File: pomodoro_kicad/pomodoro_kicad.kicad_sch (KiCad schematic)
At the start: 48 parts, among them J1 LiPO PH2.0, J10 LED_VCC, J11 LED_DATA, J12 LED_GND, J2 Conn_01x04, J3 VDD, J4 GND, J5 SCK, J6 WS, J7 SD, J8 L/R, J9 USB_C_Receptacle_USB2.0_16P, Q1 IRLML6402, SW1 RotaryEncoder_Switch, U1 AP2112K-3.3, U2 MCP73831-2-OT, U3 ESP32-S3-WROOM-1-N16R8

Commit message: Assign footprints with actual parts
assigned:
- capacitors
- LEDs
- diode
- resistors
- push button
- usb receptacle
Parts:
- removed C13: 220uF, Capacitor_SMD:C_0603_1608Metric, symbol Device:C_Small
- added C14: 220uF, Capacitor_SMD:CP_Elec_6.3x7.7, symbol Device:C_Polarized_Small
- C1, C10, C11, C12, C2, C3, C4, C6, C7, C8, C9: footprint Capacitor_SMD:C_0603_1608Metric -> Capacitor_SMD:C_0402_1005Metric
- C5: value 100nF -> 0.1uF; footprint Capacitor_SMD:C_0603_1608Metric -> Capacitor_SMD:C_0402_1005Metric
- D3: footprint Diode_SMD:D_SMA -> Diode_SMD:D_SOD-123F
- J9: footprint Connector_USB:USB_C_Receptacle_HRO_TYPE-C-31-M-12 -> _Footprints:SAMESKY_UJ20-C-H-G-SMT-1-P16-TR
- SW1: footprint customFootprints:rotaryEncoder -> _Footprints:rotaryEncoder
- SW2, SW3: footprint Button_Switch_SMD:SW_SPST_PTS645Sx43SMTR92 -> Button_Switch_SMD:SW_Tactile_SPST_NO_Straight_CK_PTS636Sx25SMTRLFS
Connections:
- net GND: now also C14.2
- net VSYS: now also C14.1
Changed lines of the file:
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@@
 			)
 		)
-		(property "Footprint" "customFootprints:rotaryEncoder"
+		(property "Footprint" "_Footprints:rotaryEncoder"
 			(at 44.704 162.56 0)
 			(hide yes)
@@
 			)
 		)
-		(property "Footprint" "Button_Switch_SMD:SW_SPST_PTS645Sx43SMTR92"
+		(property "Footprint" "Button_Switch_SMD:SW_Tactile_SPST_NO_Straight_CK_PTS636Sx25SMTRLFS"
 			(at 86.36 69.85 0)
 			(hide yes)
@@
 			)
 		)
-		(property "Footprint" "Capacitor_SMD:C_0603_1608Metric"
+		(property "Footprint" "Capacitor_SMD:C_0402_1005Metric"
 			(at 119.38 156.21 0)
 			(hide yes)
@@
 			)
 		)
-		(property "Footprint" "Capacitor_SMD:C_0603_1608Metric"
+		(property "Footprint" "Capacitor_SMD:C_0402_1005Metric"
 			(at 95.25 27.94 0)
 			(hide yes)
@@
 			)
 		)
-		(property "Footprint" "Capacitor_SMD:C_0603_1608Metric"
+		(property "Footprint" "Capacitor_SMD:C_0402_1005Metric"
 			(at 26.67 57.15 0)
 			(hide yes)
@@
 			)
 		)
-		(property "Value" "100nF"
+		(property "Value" "0.1uF"
 			(at 40.894 187.452 90)
 			(show_name no)
@@
 			)
 		)
-		(property "Footprint" "Capacitor_SMD:C_0603_1608Metric"
+		(property "Footprint" "Capacitor_SMD:C_0402_1005Metric"
 			(at 43.18 182.88 0)
 			(hide yes)
@@
 			)
 		)
-		(property "Footprint" "Capacitor_SMD:C_0603_1608Metric"
+		(property "Footprint" "Capacitor_SMD:C_0402_1005Metric"
 			(at 24.13 158.75 0)
 			(hide yes)
@@
 			)
 		)
-		(property "Footprint" "Capacitor_SMD:C_0603_1608Metric"
+		(property "Footprint" "Capacitor_SMD:C_0402_1005Metric"
 			(at 26.67 64.77 0)
 			(hide yes)
@@
 			)
 		)
-		(property "Footprint" "Capacitor_SMD:C_0603_1608Metric"
+		(property "Footprint" "Capacitor_SMD:C_0402_1005Metric"
 			(at 22.86 87.63 0)
 			(hide yes)
@@
 			)
 		)
-		(property "Footprint" "Capacitor_SMD:C_0603_1608Metric"
+		(property "Footprint" "Capacitor_SMD:C_0402_1005Metric"
 			(at 104.14 149.86 0)
 			(hide yes)
@@
 			)
 		)
-		(property "Footprint" "Connector_USB:USB_C_Receptacle_HRO_TYPE-C-31-M-12"
+		(property "Footprint" "_Footprints:SAMESKY_UJ20-C-H-G-SMT-1-P16-TR"
 			(at 143.51 40.64 0)
 			(hide yes)
@@
 			)
 		)
-		(property "Footprint" "Capacitor_SMD:C_0603_1608Metric"
+		(property "Footprint" "Capacitor_SMD:C_0402_1005Metric"
 			(at 86.36 60.96 0)
 			(hide yes)
@@
 			)
 		)
-		(property "Footprint" "Diode_SMD:D_SMA"
+		(property "Footprint" "Diode_SMD:D_SOD-123F"
 			(at 164.465 96.52 0)
 			(hide yes)
@@
 	)
 	(symbol
+		(lib_id "Device:C_Polarized_Small")
+		(at 208.28 22.86 0)
+		(unit 1)
+		(body_style 1)
+		(exclude_from_sim no)
+		(in_bom yes)
+		(on_board yes)
+		(in_pos_files yes)
+		(dnp no)
+		(fields_autoplaced yes)
+		(property "Reference" "C14"
+			(at 210.82 21.0438 0)
+			(show_name no)
+			(do_not_autoplace no)
+			(effects
+				(font
+					(size 1.27 1.27)
+				)
+				(justify left)
+			)
+		)
+		(property "Value" "220uF"
+			(at 210.82 23.5838 0)
+			(show_name no)
+			(do_not_autoplace no)
+			(effects
+				(font
+					(size 1.27 1.27)
+				)
+				(justify left)
+			)
+		)
+		(property "Footprint" "Capacitor_SMD:CP_Elec_6.3x7.7"
+			(at 208.28 22.86 0)
+			(hide yes)
+			(show_name no)
+			(do_not_autoplace no)
+			(effects
+				(font
+					(size 1.27 1.27)
+				)
+			)
+		)
+		(property "Datasheet" ""
+			(at 208.28 22.86 0)
+			(hide yes)
+			(show_name no)
+			(do_not_autoplace no)
+			(effects
+				(font
+					(size 1.27 1.27)
+				)
+			)
+		)
+		(property "Description" "Polarized capacitor, small symbol"
+			(at 208.28 22.86 0)
+			(hide yes)
+			(show_name no)
+			(do_not_autoplace no)
+			(effects
+				(font
+					(size 1.27 1.27)
+				)
+			)
+		)
+		(pin "1"
+		)
+		(pin "2"
+		)
+		(instances
+			(project "pomodoro_kicad"
+				(path "/10c5c50b-7fce-4167-a001-e0e180833e3a"
+					(reference "C14")
+					(unit 1)
+				)
+			)
+		)
+	)
+	(symbol
 		(lib_id "Device:C_Small")
 		(at 86.36 78.74 270)
@@
 			)
 		)
-		(property "Footprint" "Capacitor_SMD:C_0603_1608Metric"
+		(property "Footprint" "Capacitor_SMD:C_0402_1005Metric"
 			(at 86.36 78.74 0)
 			(hide yes)
@@
 			)
 		)
-		(property "Footprint" "Capacitor_SMD:C_0603_1608Metric"
+		(property "Footprint" "Capacitor_SMD:C_0402_1005Metric"
 			(at 64.77 27.94 0)
 			(hide yes)
@@
 	)
 	(symbol
-		(lib_id "Device:C_Small")
-		(at 208.28 22.86 0)
-		(unit 1)
-		(body_style 1)
-		(exclude_from_sim no)
-		(in_bom yes)
-		(on_board yes)
-		(in_pos_files yes)
-		(dnp no)
-		(fields_autoplaced yes)
-		(property "Reference" "C13"
-			(at 210.82 21.5899 0)
-			(show_name no)
-			(do_not_autoplace no)
-			(effects
-				(font
-					(size 1.27 1.27)
-				)
-				(justify left)
-			)
-		)
-		(property "Value" "220uF"
-			(at 210.82 24.1299 0)
-			(show_name no)
-			(do_not_autoplace no)
-			(effects
-				(font
-					(size 1.27 1.27)
-				)
-				(justify left)
-			)
-		)
-		(property "Footprint" "Capacitor_SMD:C_0603_1608Metric"
-			(at 208.28 22.86 0)
-			(hide yes)
-			(show_name no)
-			(do_not_autoplace no)
-			(effects
-				(font
-					(size 1.27 1.27)
-				)
-			)
-		)
-		(property "Datasheet" ""
-			(at 208.28 22.86 0)
-			(hide yes)
-			(show_name no)
-			(do_not_autoplace no)
-			(effects
-				(font
-					(size 1.27 1.27)
-				)
-			)
-		)
-		(property "Description" "Unpolarized capacitor, small symbol"
-			(at 208.28 33.02 0)
-			(hide yes)
-			(show_name no)
-			(do_not_autoplace no)
-			(effects
-				(font
-					(size 1.27 1.27)
-				)
-			)
-		)
-		(pin "2"
-		)
-		(pin "1"
-		)
-		(instances
-			(project "pomodoro_kicad"
-				(path "/10c5c50b-7fce-4167-a001-e0e180833e3a"
-					(reference "C13")
-					(unit 1)
-				)
-			)
-		)
-	)
-	(symbol
 		(lib_id "power:GND")
 		(at 48.26 182.88 0)
@@
 			)
 		)
-		(property "Footprint" "Button_Switch_SMD:SW_SPST_PTS645Sx43SMTR92"
+		(property "Footprint" "Button_Switch_SMD:SW_Tactile_SPST_NO_Straight_CK_PTS636Sx25SMTRLFS"
 			(at 86.36 52.07 0)
 			(hide yes)
@@
 			)
 		)
-		(property "Footprint" "Capacitor_SMD:C_0603_1608Metric"
+		(property "Footprint" "Capacitor_SMD:C_0402_1005Metric"
 			(at 57.15 160.02 0)
 			(hide yes)

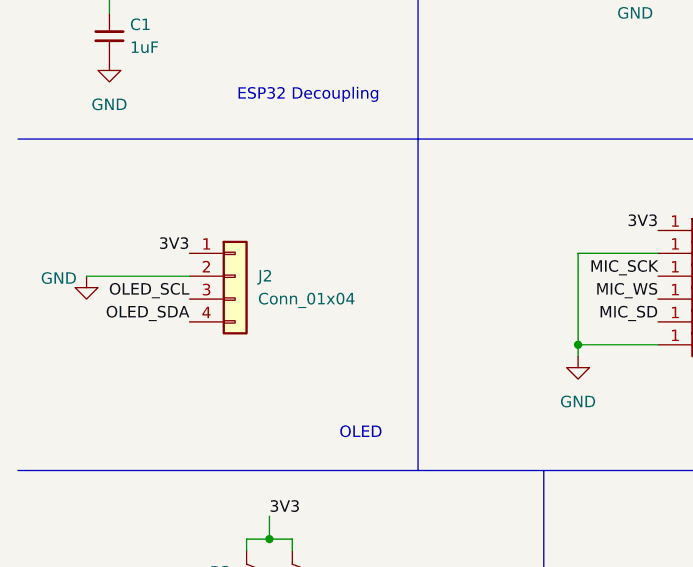
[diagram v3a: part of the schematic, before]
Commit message: Finish assigning footprints
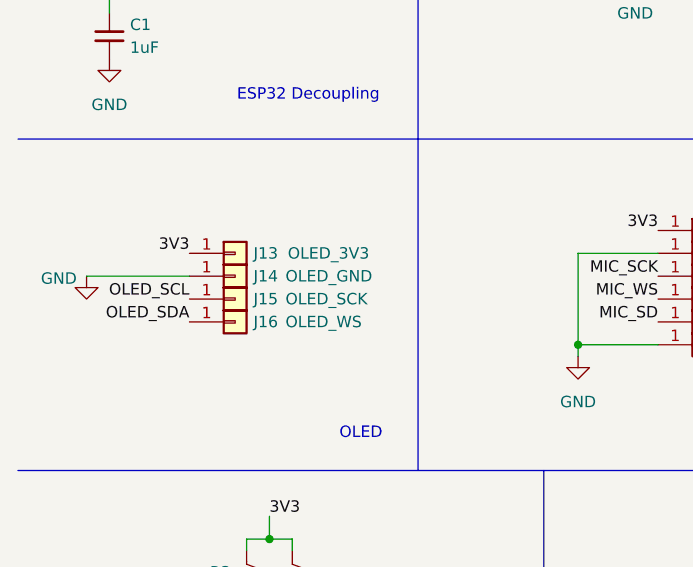
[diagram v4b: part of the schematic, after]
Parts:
- removed J2: Conn_01x04, Connector_PinSocket_2.54mm:PinSocket_1x04_P2.54mm_Vertical, symbol Connector_Generic:Conn_01x04
- added J13: OLED_3V3, TestPoint:TestPoint_THTPad_D2.0mm_Drill1.0mm, symbol Connector_Generic:Conn_01x01
- added J14: OLED_GND, TestPoint:TestPoint_THTPad_D2.0mm_Drill1.0mm, symbol Connector_Generic:Conn_01x01
- added J15: OLED_SCK, TestPoint:TestPoint_THTPad_D2.0mm_Drill1.0mm, symbol Connector_Generic:Conn_01x01
- added J16: OLED_WS, TestPoint:TestPoint_THTPad_D2.0mm_Drill1.0mm, symbol Connector_Generic:Conn_01x01
- J1: footprint Connector_JST:JST_PH_B2B-PH-K_1x02_P2.00mm_Vertical -> Connector_JST:JST_PH_S2B-PH-SM4-TB_1x02-1MP_P2.00mm_Horizontal
- Q1: footprint Package_TO_SOT_SMD:SOT-23 -> Package_TO_SOT_SMD:SOT-23-3
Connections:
- net 3V3: now also J13.1 (Pin_1)
- net GND: now also J14.1 (Pin_1)
- net OLED_SCL: now also J15.1 (Pin_1)
- net OLED_SDA: now also J16.1 (Pin_1)

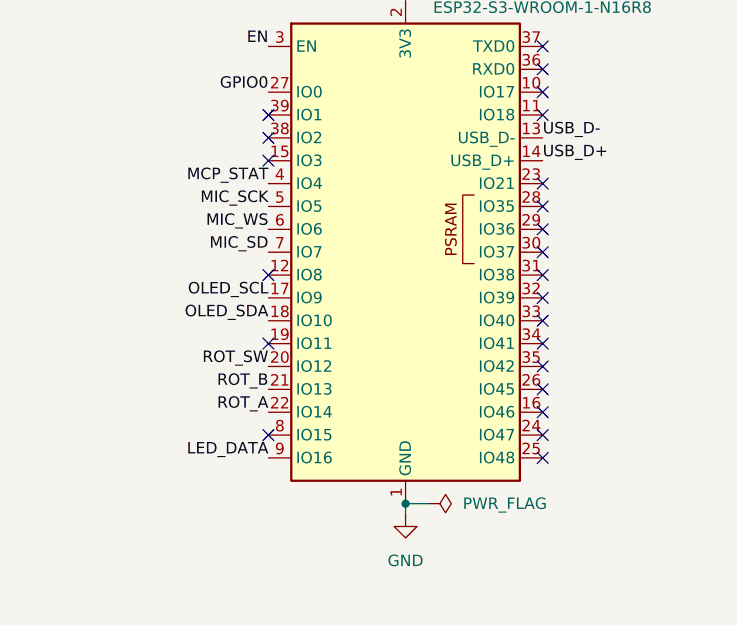
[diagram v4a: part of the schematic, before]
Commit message: Route PCB and update schematic pins for better connections
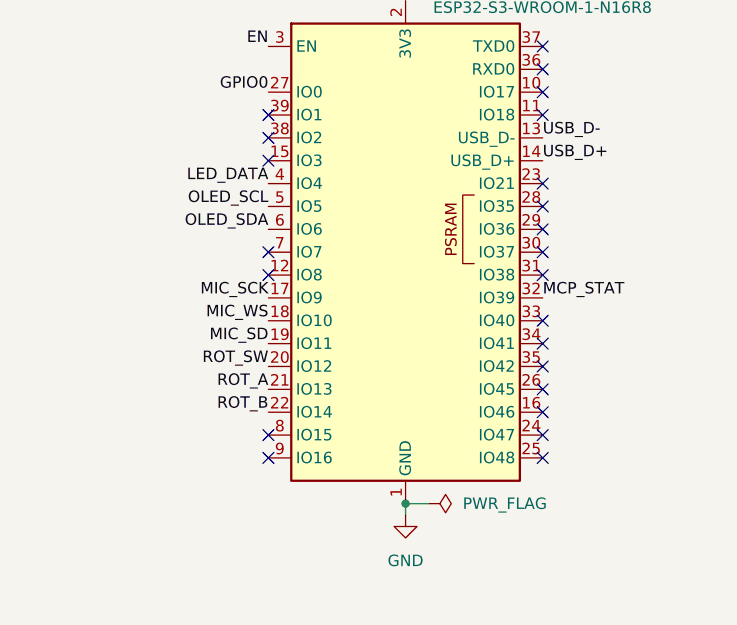
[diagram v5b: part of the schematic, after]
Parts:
- J9: footprint _Footprints:SAMESKY_UJ20-C-H-G-SMT-1-P16-TR -> Connector_USB:USB_C_Receptacle_HRO_TYPE-C-31-M-12
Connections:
- net LED_DATA: now also U3.4 (IO4); no longer U3.9 (IO16)
- net MCP_STAT: now also U3.32 (IO39); no longer U3.4 (IO4)
- net MIC_SCK: now also U3.17 (IO9); no longer U3.5 (IO5)
- net MIC_SD: now also U3.19 (IO11); no longer U3.7 (IO7)
- net MIC_WS: now also U3.18 (IO10); no longer U3.6 (IO6)
- net OLED_SCL: now also U3.5 (IO5); no longer U3.17 (IO9)
- net OLED_SDA: now also U3.6 (IO6); no longer U3.18 (IO10)
- net ROT_A: now also U3.21 (IO13); no longer U3.22 (IO14)
- net ROT_B: now also U3.22 (IO14); no longer U3.21 (IO13)
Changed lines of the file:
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@@
 	)
 	(no_connect
-		(at 224.79 137.16)
+		(at 224.79 129.54)
 	)
 	(no_connect
-		(at 224.79 129.54)
+		(at 224.79 127)
 	)
 	(no_connect
-		(at 255.27 134.62)
+		(at 224.79 147.32)
 	)
 	(no_connect
-		(at 224.79 114.3)
+		(at 255.27 134.62)
 	)
 	(no_connect
-		(at 224.79 147.32)
+		(at 224.79 149.86)
 	)
 	(no_connect
-		(at 255.27 132.08)
+		(at 224.79 114.3)
 	)
 	(no_connect
@@
 	)
 	(label "ROT_B"
-		(at 224.79 142.24 180)
+		(at 224.79 144.78 180)
 		(effects
 			(font
@@
 	)
 	(label "MIC_SCK"
-		(at 224.79 121.92 180)
+		(at 224.79 132.08 180)
 		(effects
 			(font
@@
 	)
 	(label "OLED_SDA"
-		(at 224.79 134.62 180)
+		(at 224.79 124.46 180)
 		(effects
 			(font
@@
 	)
 	(label "OLED_SCL"
-		(at 224.79 132.08 180)
+		(at 224.79 121.92 180)
 		(effects
 			(font
@@
 	)
 	(label "MIC_WS"
-		(at 224.79 124.46 180)
+		(at 224.79 134.62 180)
 		(effects
 			(font
@@
 	)
 	(label "ROT_A"
-		(at 224.79 144.78 180)
+		(at 224.79 142.24 180)
 		(effects
 			(font
@@
 	)
 	(label "LED_DATA"
-		(at 224.79 149.86 180)
+		(at 224.79 119.38 180)
 		(effects
 			(font
@@
 	)
 	(label "MCP_STAT"
-		(at 224.79 119.38 180)
+		(at 255.27 132.08 0)
 		(effects
 			(font
 				(size 1.27 1.27)
 			)
-			(justify right bottom)
+			(justify left bottom)
 		)
 	)
@@
 	)
 	(label "MIC_SD"
-		(at 224.79 127 180)
+		(at 224.79 137.16 180)
 		(effects
 			(font
@@
 			)
 		)
-		(property "Footprint" "_Footprints:SAMESKY_UJ20-C-H-G-SMT-1-P16-TR"
+		(property "Footprint" "Connector_USB:USB_C_Receptacle_HRO_TYPE-C-31-M-12"
 			(at 143.51 40.64 0)
 			(hide yes)
